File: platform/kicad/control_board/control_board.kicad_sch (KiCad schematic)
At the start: 40 parts, among them J1 DHT22, J10 ADC1,7, J11 Qwiic JST, J16 Conn_01x05_Pin, J2 DS18B20, J8 UART, J9 ADC1,6, K1 LCA717, K2 LCA717, K3 LCA717, K4 LCA717, U1 ESP32-DevKitC

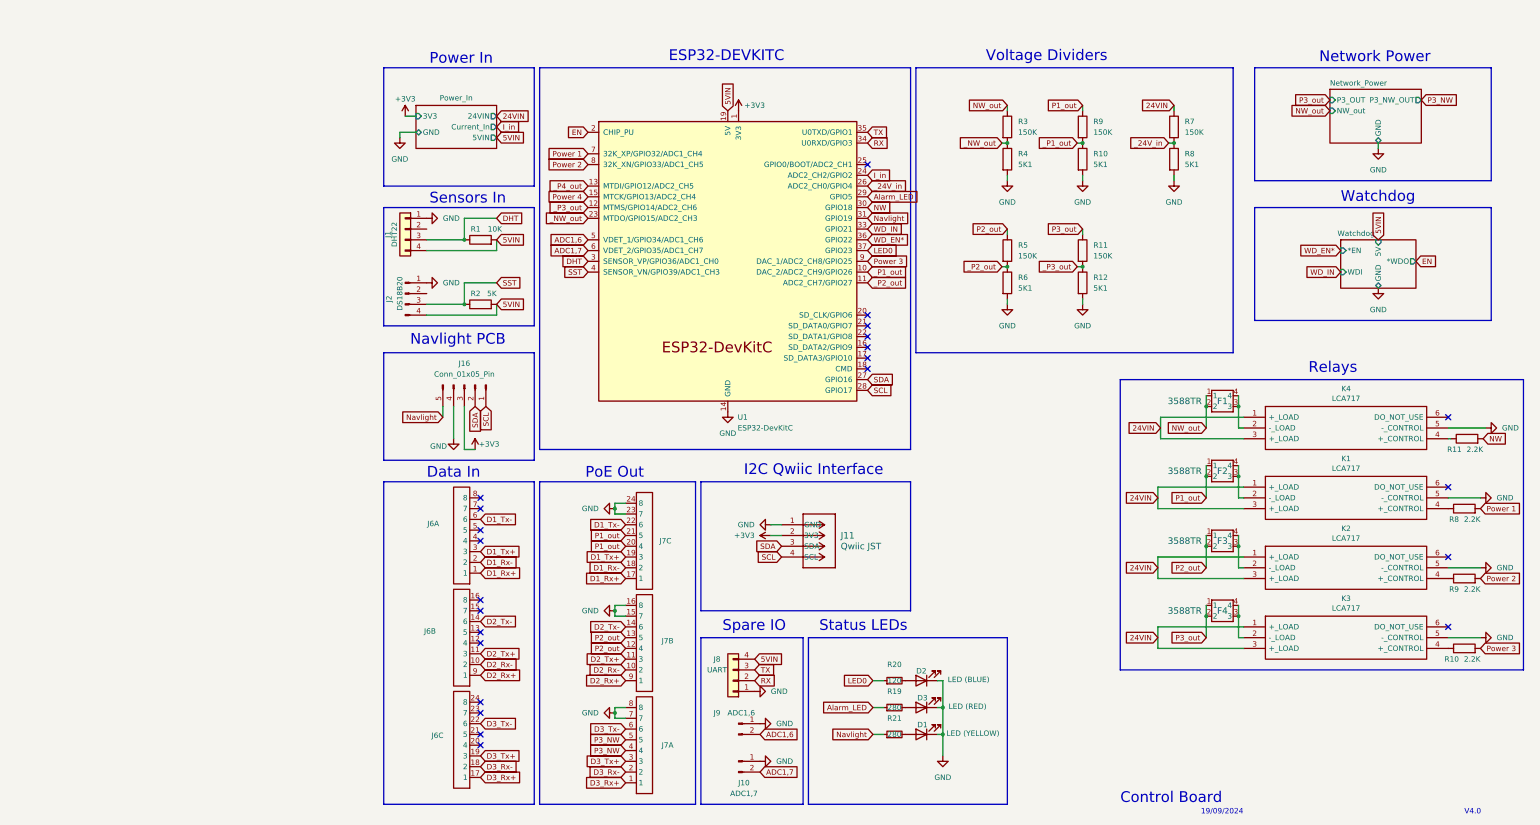
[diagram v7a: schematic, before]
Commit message: Control_PCB v4 revB: Finalised Design
This change updates the controller PCB to a finalised state, only requiring
finishing touches to be made for manufacturing.
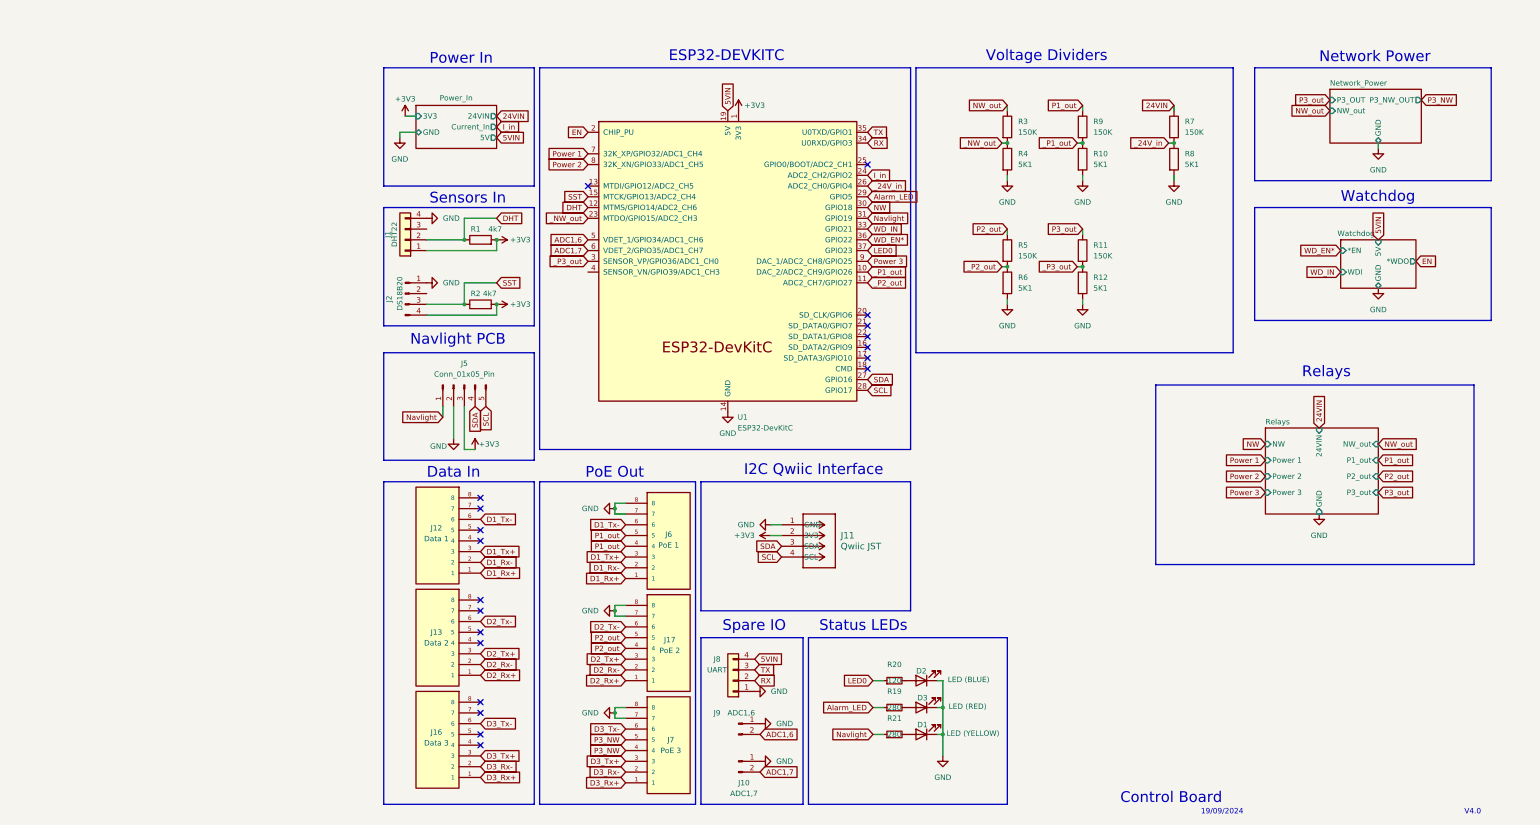
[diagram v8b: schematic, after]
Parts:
- removed F1, F2, F3, F4: 3588TR, AusOcean:3588TR_FUSE_HOLDER, symbol AusOcean:3588TR
- removed J16: Conn_01x05_Pin, Connector_JST:JST_SH_SM05B-SRSS-TB_1x05-1MP_P1.00mm_Horizontal, symbol Connector:Conn_01x05_Pin
- removed J6, J7: ~, AusOcean:RJ45 3-port jack, symbol AusOcean:RJ45_3-port_jack
- removed K1, K2, K3, K4: LCA717, AusOcean:LCA717_Relay_Holder, symbol AusOceanPCB-rescue:LCA717-MISC
- removed R10, R11, R8, R9: 2.2K, Resistor_SMD:R_0201_0603Metric, symbol Device:R
- added J12: Data 1, AusOcean:CONNFLY Elec DS1128-05-S8B8P, symbol AusOcean:CRJ032-1-TH
- added J13: Data 2, AusOcean:CONNFLY Elec DS1128-05-S8B8P, symbol AusOcean:CRJ032-1-TH
- added J16: Data 3, AusOcean:CONNFLY Elec DS1128-05-S8B8P, symbol AusOcean:CRJ032-1-TH
- added J17: PoE 2, AusOcean:CONNFLY Elec DS1128-05-S8B8P, symbol AusOcean:CRJ032-1-TH
- added J5: Conn_01x05_Pin, Connector_JST:JST_SH_SM05B-SRSS-TB_1x05-1MP_P1.00mm_Horizontal, symbol Connector:Conn_01x05_Pin
- added J6: PoE 1, AusOcean:CONNFLY Elec DS1128-05-S8B8P, symbol AusOcean:CRJ032-1-TH
- added J7: PoE 3, AusOcean:CONNFLY Elec DS1128-05-S8B8P, symbol AusOcean:CRJ032-1-TH
- R1: value 10K -> 4k7
- R2: value 5K -> 4k7
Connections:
- net Power 4 is gone; now on net SST: U1.15 (MTCK/GPIO13/ADC2_CH4)
- net +3V3: now also J1.1 (Pin_1), J2.4 (Pin_4), R1.2, R2.2, J5.3 (Pin_3)
- net 5VIN: no longer J1.4 (Pin_4), J2.4 (Pin_4), R1.2, R2.2
- net D1_Rx+: now also J12.1, J6.1
- net D1_Rx-: now also J12.2, J6.2
- net D1_Tx+: now also J12.3, J6.3
- net D1_Tx-: now also J12.6, J6.6
- net D2_Rx+: now also J13.1, J17.1
- net D2_Rx-: now also J13.2, J17.2
- net D2_Tx+: now also J13.3, J17.3
- net D2_Tx-: now also J13.6, J17.6
- net D3_Rx+: now also J16.1, J7.1
- net D3_Rx-: now also J16.2, J7.2
- net D3_Tx+: now also J16.3, J7.3
- net D3_Tx-: now also J16.6, J7.6
- net DHT: now also J1.2 (Pin_2), U1.12 (MTMS/GPIO14/ADC2_CH6); no longer J1.3 (Pin_3), U1.3 (SENSOR_VP/GPIO36/ADC1_CH0)
- net GND: now also J1.4 (Pin_4), J17.7, J17.8, J5.2 (Pin_2), J6.7, J6.8, J7.7, J7.8; no longer J1.1 (Pin_1)
- net Navlight: now also J5.1 (Pin_1)
- net P1_out: now also J6.4, J6.5
- net P2_out: now also J17.4, J17.5
- net P3_NW: now also J7.4, J7.5
- net SCL: now also J5.5 (Pin_5)
- net SDA: now also J5.4 (Pin_4)
- net SST: no longer U1.4 (SENSOR_VN/GPIO39/ADC1_CH3)
- net _P3_out: now also U1.3 (SENSOR_VP/GPIO36/ADC1_CH0); no longer U1.12 (MTMS/GPIO14/ADC2_CH6)
- net _P4_out: no longer names the net of U1.13 (MTDI/GPIO12/ADC2_CH5)
- no-connect marks 23 -> 20
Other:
- added sheet Relays (relays.kicad_sch)
- sheet Power_In ports: added 5V; removed 5VIN
